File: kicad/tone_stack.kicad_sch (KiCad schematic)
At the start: 4 parts

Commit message: Datasheet footprints, floor-plan placement, headless autoroute (144/145, DRC 0)
PCB-AUDIT s1 fixes with datasheet-derived project footprints:
- TO-220-5_Vertical_P1.70mm_LM1875 (TI NDH0005D): 1.45 mm pads on the 1.1 mm
  drill -> 0.175 mm annular (was 0.0875, 5 DRC errors); pad-local 0.2 mm clearance
- Bridge_KBP_P3.81mm (Diodes DS39310 KBP404G-KBP410G, pins + ~ ~ -); bridge
  symbol renumbered to the physical order; errata #3 updated (KBU needs a swap)
- value-aware CP/R sizing (real can sizes for 4700/2200/1000 uF, 5 W / 1 W
  resistors, fat pads on the 0R speaker return); Part 4 wire pads for all
  off-board wiring (2.0 mm/1.2 mm signal, 3.0 mm/1.5 mm speaker + transformer)
- VRAW/AC1/AC2 moved into the HighCurrent net class (errata #11)

gen_pcb.py now places to the Part 5 floor plan: balanced columns (Input/Preamp
with Tone stacked below | Reverb/Trem/MRB | Power Amp | PSU), signal order inside
zones with serpentine shelves, LM1875/LM317 on the top edge with the 10 mm
keep-out, wiring edge along the bottom, 4x M3 holes, two locked 0.9 mm escape
stubs off the LM1875 pins 4/5 (a 1.5/2.5 mm trace cannot enter a 1.70 mm pitch).
DRC before routing: 0 errors, 0 warnings.

route_board.py: pcbnew DSN export -> Freerouting -> SES import -> pour refill.
Freerouting 2.1.0 ignores every pass/timeout limit in CLI mode and only writes
output at 0 unrouted (and its MT router crashed), so the script drives 1.9.0
under xvfb-run and injects autoroute_settings (bottom layer 6x cost, via 80) so
the GND pour stays whole. Committed board: 144/145 connections routed, 0 DRC
violations (--severity-all), 26 vias, 351 mm on the bottom vs 3.7 m on top; the
one open PA_OUT link (blocked by R_bias1) is documented as a GUI finish.

Chassis-fit figure corrected: the old 48-53 % / 82-90 % densities counted hidden
text boxes; text-less it is ~33 % on 190x115 and ~56 % on 155x90.

Docs: PCB-NOTES/PCB-AUDIT rewritten, README, CHANGELOG, errata #3/#11,
SOURCES (package drawings), Part 10, kicad RE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
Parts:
- POT_TONE, POT_VOL: footprint Connector_PinHeader_2.54mm:PinHeader_1x03_P2.54mm_Vertical -> cambridge_reverb:WirePad_1x03_P2.54mm_D1.2mm
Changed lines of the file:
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@@
     (property "Reference" "POT_VOL" (at 154.93999999999997 116.83999999999999 0) (effects (font (size 1.27 1.27)) (justify left)))
     (property "Value" "250k log" (at 154.93999999999997 119.38 0) (effects (font (size 1.27 1.27)) (justify left)))
-    (property "Footprint" "Connector_PinHeader_2.54mm:PinHeader_1x03_P2.54mm_Vertical" (at 152.39999999999998 124.46 0) (effects (font (size 1.27 1.27)) hide))
+    (property "Footprint" "cambridge_reverb:WirePad_1x03_P2.54mm_D1.2mm" (at 152.39999999999998 124.46 0) (effects (font (size 1.27 1.27)) hide))
     (pin "1")
     (pin "3")
     (pin "2")
-    (instances (project "cambridge_reverb" (path "/8498102f-cbb6-4d6d-8501-63c9f701fd70" (reference "POT_VOL") (unit 1))))
+    (instances (project "cambridge_reverb" (path "/dd2392ab-c100-4028-9288-d1053a5f3a13" (reference "POT_VOL") (unit 1))))
   )
   (wire (pts (xy 147.32 124.46) (xy 144.78 124.46)) (stroke (width 0) (type default)))
@@
     (pin "1")
     (pin "2")
-    (instances (project "cambridge_reverb" (path "/8498102f-cbb6-4d6d-8501-63c9f701fd70" (reference "R_fx_pad") (unit 1))))
+    (instances (project "cambridge_reverb" (path "/dd2392ab-c100-4028-9288-d1053a5f3a13" (reference "R_fx_pad") (unit 1))))
   )
   (wire (pts (xy 147.32 165.1) (xy 144.78 165.1)) (stroke (width 0) (type default)))
@@
     (pin "1")
     (pin "2")
-    (instances (project "cambridge_reverb" (path "/8498102f-cbb6-4d6d-8501-63c9f701fd70" (reference "C_cut") (unit 1))))
+    (instances (project "cambridge_reverb" (path "/dd2392ab-c100-4028-9288-d1053a5f3a13" (reference "C_cut") (unit 1))))
   )
   (wire (pts (xy 217.16999999999996 124.46) (xy 214.63 124.46)) (stroke (width 0) (type default)))
@@
     (property "Reference" "POT_TONE" (at 270.51 116.83999999999999 0) (effects (font (size 1.27 1.27)) (justify left)))
     (property "Value" "100k lin" (at 270.51 119.38 0) (effects (font (size 1.27 1.27)) (justify left)))
-    (property "Footprint" "Connector_PinHeader_2.54mm:PinHeader_1x03_P2.54mm_Vertical" (at 267.96999999999997 124.46 0) (effects (font (size 1.27 1.27)) hide))
+    (property "Footprint" "cambridge_reverb:WirePad_1x03_P2.54mm_D1.2mm" (at 267.96999999999997 124.46 0) (effects (font (size 1.27 1.27)) hide))
     (pin "1")
     (pin "3")
     (pin "2")
-    (instances (project "cambridge_reverb" (path "/8498102f-cbb6-4d6d-8501-63c9f701fd70" (reference "POT_TONE") (unit 1))))
+    (instances (project "cambridge_reverb" (path "/dd2392ab-c100-4028-9288-d1053a5f3a13" (reference "POT_TONE") (unit 1))))
   )
   (wire (pts (xy 262.89 124.46) (xy 260.34999999999997 124.46)) (stroke (width 0) (type default)))

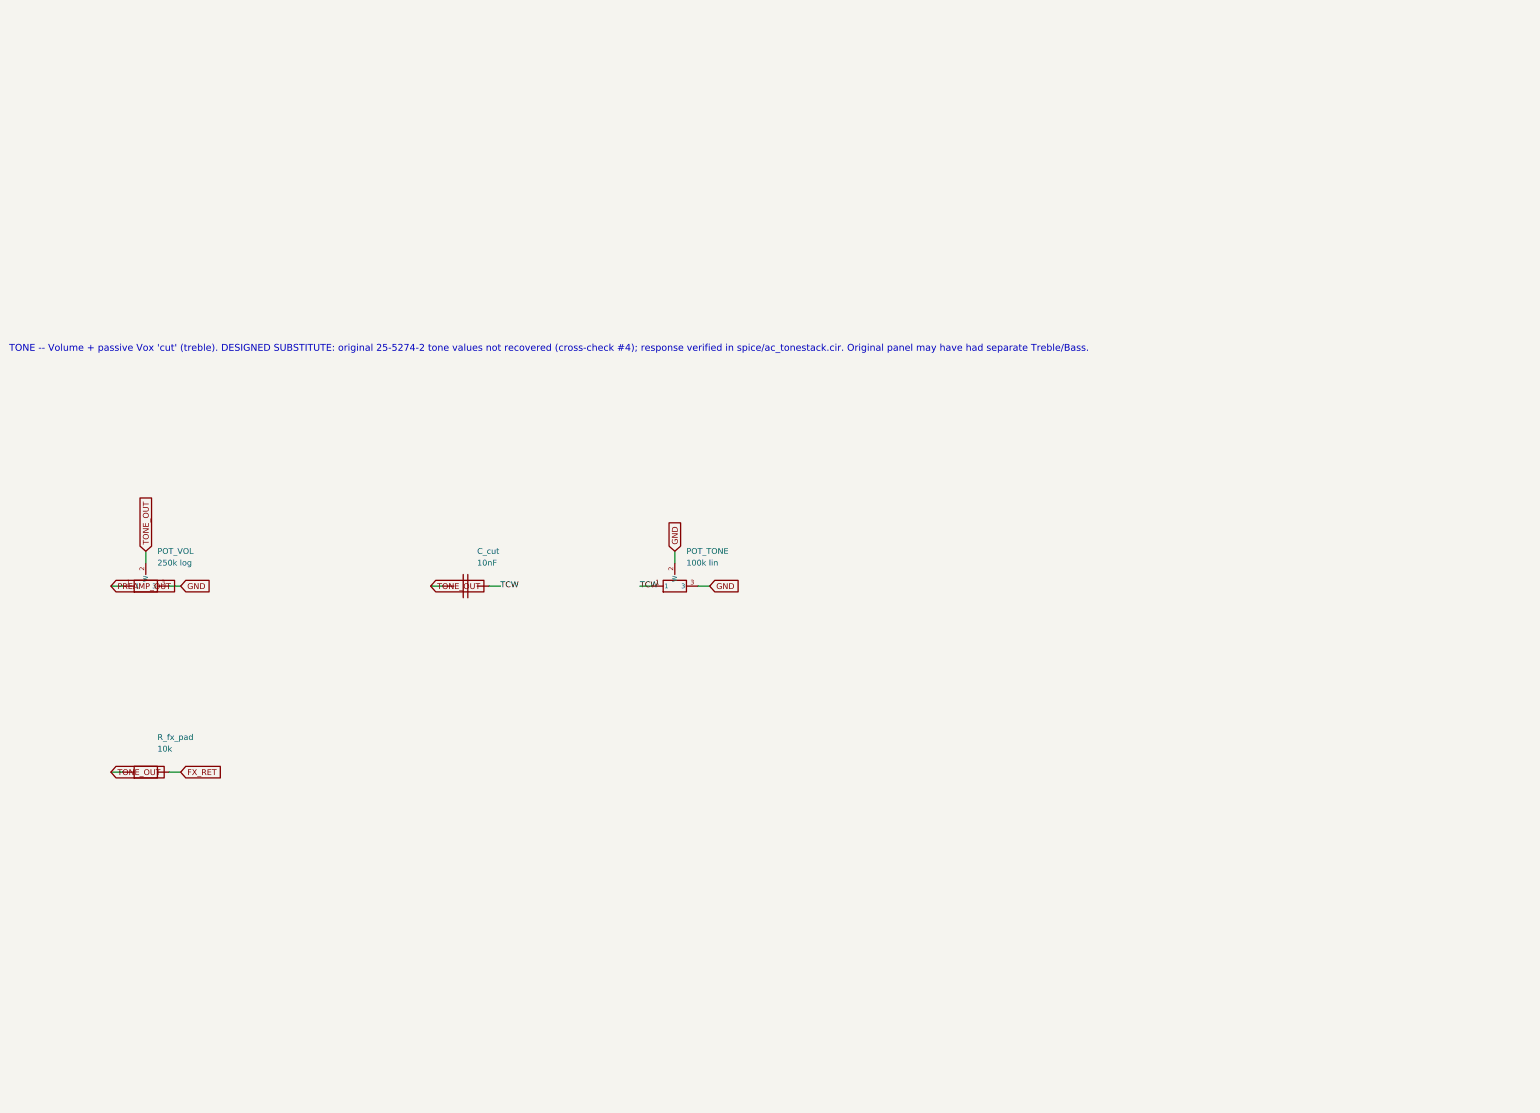
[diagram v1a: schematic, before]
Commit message: Add 26 labelled bench test points (schematic + BOM + silk) and re-route
Test points follow the Part 5 bring-up order: rails (VRAW, +33V5, VREG_IN,
+17V), JFET drains Q1D/Q2D/QRD (the errata #15 bias trim), the VBIAS_R/VBIAS_T
mid-rail refs, every inter-stage node (PREAMP_OUT, TONE_OUT, BLEND, TREM_OUT,
MRB_OUT, PA_IN), tank drive/return, LFO, PA_BIAS/PA_OUT/SPK_P, and a GND pin
per zone for the probe clip.

- gen_kicad.py: one-pin TP symbol; TEST_POINTS table; add_test_points() puts
  them on their sheets so they are in the netlist and the BOM (one order line)
- footprint TestPoint_THT_D2.0mm_Label: 2.0 mm pad / 1.0 mm drill for a header
  pin or wire loop; the footprint VALUE (= net alias) prints on F.SilkS
- gen_pcb.py: test-point strip across the top of each zone; the effects column
  is now two stacked zones (tremolo+MRB above, reverb below next to its tank
  pads) so each block's points sit right above its parts; stacked-zone gap 2 mm
- PCB-NOTES.md: test-point table with expected values (Part 3 troubleshooting,
  Part 2 set-up, ngspice) and the bring-up sequence
- Re-routed (Freerouting 1.9.0, B.Cu x7, via 60): 161/166 connections, 0 DRC
  violations, 54 vias; the five open links are listed for a GUI finish

Co-Authored-By: Claude Fable 5.1 <noreply@anthropic.com>
Claude-Session: https://claude.ai/code/session_01Vk8HkvCugxFpQsBPVnNT2H
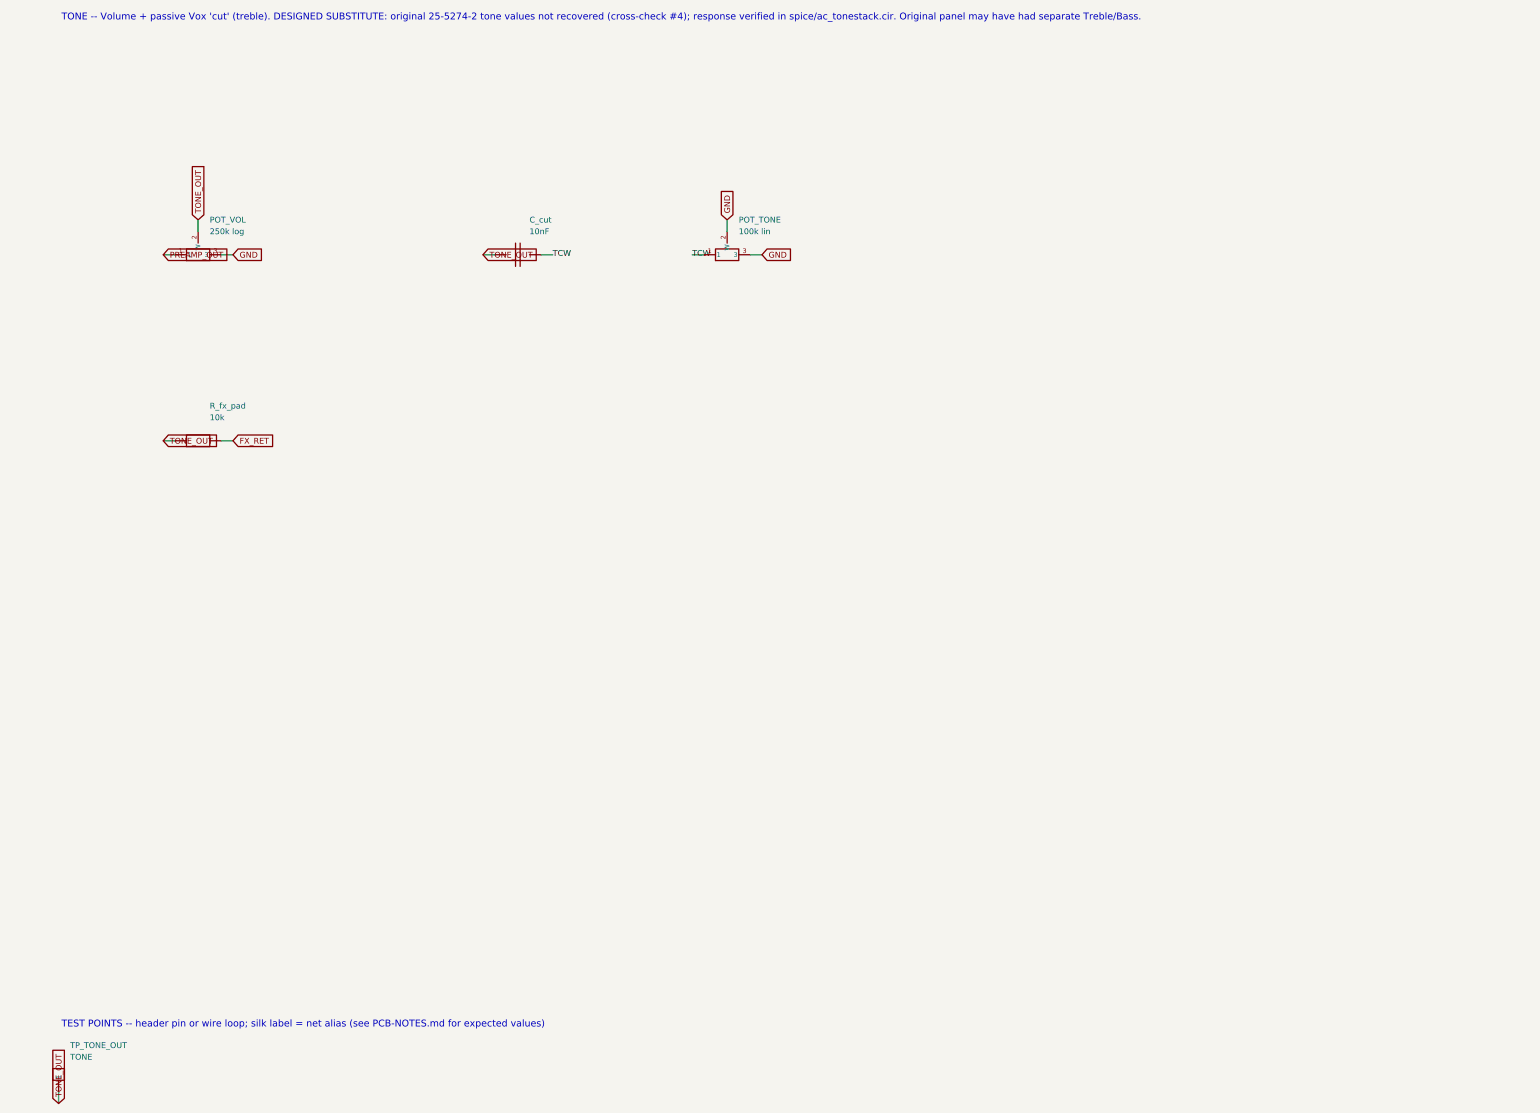
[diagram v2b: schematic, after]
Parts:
- added TP_TONE_OUT: TONE, cambridge_reverb:TestPoint_THT_D2.0mm_Label, symbol cr_primitives:TP
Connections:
- net TONE_OUT: now also TP_TONE_OUT.1
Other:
- note added: "TEST POINTS -- header pin or wire loop; silk label = net alias (see PCB-NOTES.md for expected values)"
